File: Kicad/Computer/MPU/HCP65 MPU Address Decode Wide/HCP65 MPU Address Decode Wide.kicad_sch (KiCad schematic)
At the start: 0 parts

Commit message: Regenerating some gerbers again with paste layers.  Fixed Address Decode Wide.
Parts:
- added C23 (x10): 1μF, SamacSys_Parts:C_0805, symbol HCP65:C_0805
- added C27 (x2): 10μF, SamacSys_Parts:C_0805, symbol HCP65:C_0805
- added IC1: SN74LVC3G04DCUR, SOP50P310X90-8N, symbol Texas_Instruments:SN74LVC3G04DCUR_Multi
- added IC11, IC16, IC32, IC33, IC38, IC39: 74LVC138APW-Q100J, SOP65P640X110-16N, symbol Nexperia:74LVC138APW-Q100J
- added IC2: AP7365-33WG-7, SOT95P285X130-5N, symbol Diodes_Inc:AP7365-33WG-7
- added IC34: 74LVC1G27GW,125, SOP65P210X110-6N, symbol Nexperia:74LVC1G27GW,125
- added IC37: 74LVC2G32DP,125, SOP65P400X110-8N, symbol Nexperia:74LVC2G32DP,125_Multi
- added IC40: 74LVC08APW,112, SOP65P640X110-14N, symbol Nexperia:74LVC08APW,112_Multi
- added J1, J3: Pin_Header_01x32, SamacSys_Parts:PinHeader_1x32_P2.54mm_Vertical, symbol HCP65:Pin_Header_01x32
- added J2: Conn_02x32_Counter_Clockwise, SamacSys_Parts:DIP-64_Board_W15.24mm, symbol Connector_Generic:Conn_02x32_Counter_Clockwise
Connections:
- new net: IC37.5 (2A), IC40.8 (3Y)
- new net 3.3V: C23.1, C23.1, C23.1, C23.1, C23.1, C23.1, C23.1, C23.1, C23.1, C23.1, C27.1, IC1.8 (3V), IC1.8 (3V), IC1.8 (3V), IC11.16 (3V), IC16.16 (3V), IC2.5 (VOUT), IC32.16 (3V), IC33.16 (3V), IC34.5 (3V), IC37.8 (VCC), IC37.8 (VCC), IC38.16 (3V), IC39.16 (3V), IC40.14 (3V), IC40.14 (3V), IC40.14 (3V), IC40.14 (3V)
- new net 5V: C27.1, IC2.1 (VIN), IC2.3 (EN), J2.3 (Pin_3), J2.35 (Pin_35)
- new net A0: IC38.1 (A0), IC39.1 (A0), J2.24 (Pin_24)
- new net A1: IC38.2 (A1), IC39.2 (A1), J2.22 (Pin_22)
- new net A15: IC16.1 (A0), IC32.1 (A0), J2.19 (Pin_19)
- new net A16: IC16.2 (A1), IC32.2 (A1), J2.18 (Pin_18)
- new net A17: IC16.3 (A2), IC32.3 (A2), IC33.1 (A0), J2.17 (Pin_17)
- new net A18: IC16.5 (~{E2}), IC32.6 (E3), IC33.2 (A1), J2.16 (Pin_16)
- new net A19: IC11.1 (A0), J2.15 (Pin_15)
- new net A2: IC38.3 (A2), IC39.3 (A2), J2.21 (Pin_21)
- new net A20: IC11.2 (A1), J2.14 (Pin_14)
- new net A21: IC11.3 (A2), IC34.6 (C), J2.13 (Pin_13)
- new net A22: IC11.5 (~{E2}), IC34.3 (B), J2.12 (Pin_12)
- new net A23: IC11.4 (~{E1}), IC34.1 (A), J2.11 (Pin_11)
- new net A3: IC1.3 (2A), IC38.5 (~{E2}), J2.20 (Pin_20)
- new net GND: C23.2, C23.2, C23.2, C23.2, C23.2, C23.2, C23.2, C23.2, C23.2, C23.2, C27.2, C27.2, IC1.4 (GND), IC1.4 (GND), IC1.4 (GND), IC11.8 (GND), IC16.8 (GND), IC2.2 (GND), IC32.8 (GND), IC33.3 (A2), IC33.5 (~{E2}), IC33.8 (GND), IC34.2 (GND), IC37.4 (GND), IC37.4 (GND), IC38.8 (GND), IC39.8 (GND), IC40.7 (GND), IC40.7 (GND), IC40.7 (GND), IC40.7 (GND), J2.10 (Pin_10), J2.23 (Pin_23), J2.42 (Pin_42), J2.55 (Pin_55)
- new net Kernal Mode: IC40.1 (1A), IC40.10 (3B), J2.9 (Pin_9)
- new net Kernal Mode·Native Latch: IC11.6 (E3), IC40.3 (1Y)
- new net Native Latch: IC1.1 (1A), IC40.2 (1B), IC40.4 (2A), J2.2 (Pin_2)
- new net Reset: IC1.2 (3Y), IC32.5 (~{E2})
- new net ~{A21+A22+A23}: IC34.4 (Y), IC40.9 (3A)
- new net ~{A3}: IC1.5 (2Y), IC39.5 (~{E2})
- new net ~{Device Group 128K}: IC11.12 (~{Y3}), IC33.4 (~{E1}), IC40.13 (4B), J2.7 (Pin_7)
- new net ~{Device Group 32K}: IC11.13 (~{Y2}), IC16.4 (~{E1}), IC32.4 (~{E1}), IC40.12 (4A), J2.6 (Pin_6)
- new net ~{Device _{CS}10}: IC32.13 (~{Y2}), J2.52 (Pin_52)
- new net ~{Device _{CS}11}: IC32.12 (~{Y3}), J2.51 (Pin_51)
- new net ~{Device _{CS}12}: IC32.11 (~{Y4}), J2.50 (Pin_50)
- new net ~{Device _{CS}13}: IC32.10 (~{Y5}), J2.49 (Pin_49)
- new net ~{Device _{CS}14}: IC32.9 (~{Y6}), J2.48 (Pin_48)
- new net ~{Device _{CS}15}: IC32.7 (~{Y7}), J2.47 (Pin_47)
- new net ~{Device _{CS}16}: IC33.15 (~{Y0}), J2.46 (Pin_46)
- new net ~{Device _{CS}17}: IC33.14 (~{Y1}), J2.45 (Pin_45)
- new net ~{Device _{CS}18}: IC33.13 (~{Y2}), J2.44 (Pin_44)
- new net ~{Device _{CS}19}: IC33.12 (~{Y3}), J2.43 (Pin_43)
- new net ~{Device _{CS}1}: IC16.14 (~{Y1}), J2.63 (Pin_63)
- new net ~{Device _{CS}2}: IC16.13 (~{Y2}), J2.61 (Pin_61)
- new net ~{Device _{CS}3}: IC16.12 (~{Y3}), J2.60 (Pin_60)
- new net ~{Device _{CS}4}: IC16.11 (~{Y4}), J2.59 (Pin_59)
- new net ~{Device _{CS}5}: IC16.10 (~{Y5}), J2.58 (Pin_58)
- new net ~{Device _{CS}6}: IC16.9 (~{Y6}), J2.57 (Pin_57)
- new net ~{Device _{CS}7}: IC16.7 (~{Y7}), J2.56 (Pin_56)
- new net ~{Device _{CS}8}: IC32.15 (~{Y0}), J2.54 (Pin_54)
- new net ~{Device _{CS}9}: IC32.14 (~{Y1}), J2.53 (Pin_53)
- new net ~{Device}: IC40.11 (4Y), J2.1 (Pin_1)
- new net ~{Native Latch}: IC1.7 (1Y), IC37.1 (1A), IC37.6 (2B)
- new net ~{OTHER}: IC37.3 (2Y), J2.8 (Pin_8)
- new net ~{RAM_{CS}}: IC37.7 (1Y), J2.4 (Pin_4)
- new net ~{RAM}: IC11.15 (~{Y0}), IC37.2 (1B)
- new net ~{ROM_{CS}}: IC40.6 (2Y), J2.5 (Pin_5)
- new net ~{ROM}: IC11.14 (~{Y1}), IC40.5 (2B)
- new net ~{Reset}: IC1.6 (3A), IC16.6 (E3), IC33.6 (E3), IC38.6 (E3), IC39.6 (E3), J2.62 (Pin_62)
- new net ~{SPECIAL}: IC16.15 (~{Y0}), IC38.4 (~{E1}), IC39.4 (~{E1}), J2.64 (Pin_64)
- new net ~{Special _{CS}0}: IC38.15 (~{Y0}), J2.41 (Pin_41)
- new net ~{Special _{CS}10}: IC39.13 (~{Y2}), J2.27 (Pin_27)
- new net ~{Special _{CS}11}: IC39.12 (~{Y3}), J2.28 (Pin_28)
- new net ~{Special _{CS}12}: IC39.11 (~{Y4}), J2.29 (Pin_29)
- new net ~{Special _{CS}13}: IC39.10 (~{Y5}), J2.30 (Pin_30)
- new net ~{Special _{CS}14}: IC39.9 (~{Y6}), J2.31 (Pin_31)
- new net ~{Special _{CS}15}: IC39.7 (~{Y7}), J2.32 (Pin_32)
- new net ~{Special _{CS}1}: IC38.14 (~{Y1}), J2.40 (Pin_40)
- new net ~{Special _{CS}2}: IC38.13 (~{Y2}), J2.39 (Pin_39)
- new net ~{Special _{CS}3}: IC38.12 (~{Y3}), J2.38 (Pin_38)
- new net ~{Special _{CS}4}: IC38.11 (~{Y4}), J2.37 (Pin_37)
- new net ~{Special _{CS}5}: IC38.10 (~{Y5}), J2.36 (Pin_36)
- new net ~{Special _{CS}6}: IC38.9 (~{Y6}), J2.34 (Pin_34)
- new net ~{Special _{CS}7}: IC38.7 (~{Y7}), J2.33 (Pin_33)
- new net ~{Special _{CS}8}: IC39.15 (~{Y0}), J2.25 (Pin_25)
- new net ~{Special _{CS}9}: IC39.14 (~{Y1}), J2.26 (Pin_26)
- no-connect marks 0 -> 9
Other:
- removed sheet Address Decode Board
- note added: "A19..A23 Decode"
- note added: "Device Select"
- note added: "Kernal Mode Inverse"
- note added: "Other Select"
- note added: "Power and Spares"
- note added: "Special Address Select"
- title: (none) -> MPU Address Decode Wide

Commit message: Generated Gerbers for MPU components.
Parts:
- IC1: footprint SOP50P310X90-8N -> SamacSys_Parts:SOP50P310X90-8N; Garbage (none) -> TRIPLE INVERTER GATE
- IC11, IC16, IC32, IC33, IC38, IC39: footprint SOP65P640X110-16N -> SamacSys_Parts:SOP65P640X110-16N; Garbage (none) -> 74LVC138A-Q100 - 3-to-8 line decoder/demultiplexer; inverti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
- IC2: footprint SOT95P285X130-5N -> SamacSys_Parts:SOT95P285X130-5N
- IC34: footprint SOP65P210X110-6N -> SamacSys_Parts:SOP65P210X110-6N; Garbage (none) -> 74LVC1G27 - Single 3-input NOR gate@en-us
- IC37: footprint SOP65P400X110-8N -> SamacSys_Parts:SOP65P400X110-8N; Garbage (none) -> Nexperia 74LVC2G32DP,125, Dual 2-Input OR Logic Gate, 8-Pin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
- IC40: footprint SOP65P640X110-14N -> SamacSys_Parts:SOP65P640X110-14N; Garbage (none) -> NXP 74LVC08APW,112, Quad 2-Input AND Logic Gate, 1.2 3.6 V,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

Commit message: Removed MPU copper fills.
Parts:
- IC11, IC16, IC32, IC33, IC38, IC39: Garbage 74LVC138A-Q100 - 3-to-8 line decoder/demultiplexer; inverti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 -> (none)
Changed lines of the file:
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@@
 		)
 		(property "Footprint" "SamacSys_Parts:SOP65P640X110-16N"
-			(at 357.505 191.135 0)
+			(at 358.14 191.77 0)
 			(effects
 				(font
@@
 		)
 		(property "Datasheet" "https://assets.nexperia.com/documents/data-sheet/74LVC138A_Q100.pdf"
-			(at 357.505 193.675 0)
+			(at 358.14 194.31 0)
 			(effects
 				(font
@@
 		)
 		(property "Height" "1.1"
-			(at 357.505 198.755 0)
+			(at 358.14 199.39 0)
 			(effects
 				(font
@@
 		)
 		(property "Mouser Part Number" "771-74LVC138APWQ100J"
-			(at 357.505 201.295 0)
+			(at 358.14 201.93 0)
 			(effects
 				(font
@@
 		)
 		(property "Mouser Price/Stock" "https://www.mouser.co.uk/ProductDetail/Nexperia/74LVC138APW-Q100J?qs=fi7yB2oewZnXKE82xo%252BhJQ%3D%3D"
-			(at 357.505 203.835 0)
+			(at 358.14 204.47 0)
 			(effects
 				(font
@@
 		)
 		(property "Manufacturer_Name" "Nexperia"
-			(at 357.505 206.375 0)
+			(at 358.14 207.01 0)
 			(effects
 				(font
@@
 		)
 		(property "Manufacturer_Part_Number" "74LVC138APW-Q100J"
-			(at 357.505 208.915 0)
+			(at 358.14 209.55 0)
 			(effects
 				(font
@@
 		)
 		(property "Silkscreen" "74LVC138"
-			(at 341.63 187.96 0)
-			(effects
-				(font
-					(size 1.27 1.27)
-				)
-				(hide yes)
-			)
-		)
-		(property "Garbage" "74LVC138A-Q100 - 3-to-8 line decoder/demultiplexer; inverting@en-us"
-			(at 328.93 160.655 0)
-			(effects
-				(font
-					(size 1.27 1.27)
-				)
+			(at 358.14 196.85 0)
+			(effects
+				(font
+					(size 1.27 1.27)
+				)
+				(justify left)
 				(hide yes)
 			)
@@
 		)
 		(property "Footprint" "SamacSys_Parts:SOP65P640X110-16N"
-			(at 358.775 57.785 0)
+			(at 359.41 58.42 0)
 			(effects
 				(font
@@
 		)
 		(property "Datasheet" "https://assets.nexperia.com/documents/data-sheet/74LVC138A_Q100.pdf"
-			(at 358.775 60.325 0)
+			(at 359.41 60.96 0)
 			(effects
 				(font
@@
 		)
 		(property "Height" "1.1"
-			(at 358.775 65.405 0)
+			(at 359.41 66.04 0)
 			(effects
 				(font
@@
 		)
 		(property "Mouser Part Number" "771-74LVC138APWQ100J"
-			(at 358.775 67.945 0)
+			(at 359.41 68.58 0)
 			(effects
 				(font
@@
 		)
 		(property "Mouser Price/Stock" "https://www.mouser.co.uk/ProductDetail/Nexperia/74LVC138APW-Q100J?qs=fi7yB2oewZnXKE82xo%252BhJQ%3D%3D"
-			(at 358.775 70.485 0)
+			(at 359.41 71.12 0)
 			(effects
 				(font
@@
 		)
 		(property "Manufacturer_Name" "Nexperia"
-			(at 358.775 73.025 0)
+			(at 359.41 73.66 0)
 			(effects
 				(font
@@
 		)
 		(property "Manufacturer_Part_Number" "74LVC138APW-Q100J"
-			(at 358.775 75.565 0)
+			(at 359.41 76.2 0)
 			(effects
 				(font
@@
 		)
 		(property "Silkscreen" "74LVC138"
-			(at 342.9 54.61 0)
-			(effects
-				(font
-					(size 1.27 1.27)
-				)
-				(hide yes)
-			)
-		)
-		(property "Garbage" "74LVC138A-Q100 - 3-to-8 line decoder/demultiplexer; inverting@en-us"
-			(at 330.2 27.305 0)
-			(effects
-				(font
-					(size 1.27 1.27)
-				)
+			(at 359.41 63.5 0)
+			(effects
+				(font
+					(size 1.27 1.27)
+				)
+				(justify left)
 				(hide yes)
 			)
@@
 		)
 		(property "Footprint" "SamacSys_Parts:SOP65P640X110-16N"
-			(at 173.355 74.295 0)
+			(at 173.99 74.93 0)
 			(effects
 				(font
@@
 		)
 		(property "Datasheet" "https://assets.nexperia.com/documents/data-sheet/74LVC138A_Q100.pdf"
-			(at 173.355 76.835 0)
+			(at 173.99 77.47 0)
 			(effects
 				(font
@@
 		)
 		(property "Height" "1.1"
-			(at 173.355 81.915 0)
+			(at 173.99 82.55 0)
 			(effects
 				(font
@@
 		)
 		(property "Mouser Part Number" "771-74LVC138APWQ100J"
-			(at 173.355 84.455 0)
+			(at 173.99 85.09 0)
 			(effects
 				(font
@@
 		)
 		(property "Mouser Price/Stock" "https://www.mouser.co.uk/ProductDetail/Nexperia/74LVC138APW-Q100J?qs=fi7yB2oewZnXKE82xo%252BhJQ%3D%3D"
-			(at 173.355 86.995 0)
+			(at 173.99 87.63 0)
 			(effects
 				(font
@@
 		)
 		(property "Manufacturer_Name" "Nexperia"
-			(at 173.355 89.535 0)
+			(at 173.99 90.17 0)
 			(effects
 				(font
@@
 		)
 		(property "Manufacturer_Part_Number" "74LVC138APW-Q100J"
-			(at 173.355 92.075 0)
+			(at 173.99 92.71 0)
 			(effects
 				(font
@@
 		)
 		(property "Silkscreen" "74LVC138"
-			(at 157.48 71.12 0)
-			(effects
-				(font
-					(size 1.27 1.27)
-				)
-				(hide yes)
-			)
-		)
-		(property "Garbage" "74LVC138A-Q100 - 3-to-8 line decoder/demultiplexer; inverting@en-us"
-			(at 144.78 43.815 0)
-			(effects
-				(font
-					(size 1.27 1.27)
-				)
+			(at 173.99 80.01 0)
+			(effects
+				(font
+					(size 1.27 1.27)
+				)
+				(justify left)
 				(hide yes)
 			)
@@
 		)
 		(property "Footprint" "SamacSys_Parts:SOP65P640X110-16N"
-			(at 358.775 90.805 0)
+			(at 359.41 91.44 0)
 			(effects
 				(font
@@
 		)
 		(property "Datasheet" "https://assets.nexperia.com/documents/data-sheet/74LVC138A_Q100.pdf"
-			(at 358.775 93.345 0)
+			(at 359.41 93.98 0)
 			(effects
 				(font
@@
 		)
 		(property "Height" "1.1"
-			(at 358.775 98.425 0)
+			(at 359.41 99.06 0)
 			(effects
 				(font
@@
 		)
 		(property "Mouser Part Number" "771-74LVC138APWQ100J"
-			(at 358.775 100.965 0)
+			(at 359.41 101.6 0)
 			(effects
 				(font
@@
 		)
 		(property "Mouser Price/Stock" "https://www.mouser.co.uk/ProductDetail/Nexperia/74LVC138APW-Q100J?qs=fi7yB2oewZnXKE82xo%252BhJQ%3D%3D"
-			(at 358.775 103.505 0)
+			(at 359.41 104.14 0)
 			(effects
 				(font
@@
 		)
 		(property "Manufacturer_Name" "Nexperia"
-			(at 358.775 106.045 0)
+			(at 359.41 106.68 0)
 			(effects
 				(font
@@
 		)
 		(property "Manufacturer_Part_Number" "74LVC138APW-Q100J"
-			(at 358.775 108.585 0)
+			(at 359.41 109.22 0)
 			(effects
 				(font
@@
 		)
 		(property "Silkscreen" "74LVC138"
-			(at 342.9 87.63 0)
-			(effects
-				(font
-					(size 1.27 1.27)
-				)
-				(hide yes)
-			)
-		)
-		(property "Garbage" "74LVC138A-Q100 - 3-to-8 line decoder/demultiplexer; inverting@en-us"
-			(at 330.2 60.325 0)
-			(effects
-				(font
-					(size 1.27 1.27)
-				)
+			(at 359.41 96.52 0)
+			(effects
+				(font
+					(size 1.27 1.27)
+				)
+				(justify left)
 				(hide yes)
 			)
@@
 		)
 		(property "Footprint" "SamacSys_Parts:SOP65P640X110-16N"
-			(at 357.505 224.155 0)
+			(at 358.14 224.79 0)
 			(effects
 				(font
@@
 		)
 		(property "Datasheet" "https://assets.nexperia.com/documents/data-sheet/74LVC138A_Q100.pdf"
-			(at 357.505 226.695 0)
+			(at 358.14 227.33 0)
 			(effects
 				(font
@@
 		)
 		(property "Height" "1.1"
-			(at 357.505 231.775 0)
+			(at 358.14 232.41 0)
 			(effects
 				(font
@@
 		)
 		(property "Mouser Part Number" "771-74LVC138APWQ100J"
-			(at 357.505 234.315 0)
+			(at 358.14 234.95 0)
 			(effects
 				(font
@@
 		)
 		(property "Mouser Price/Stock" "https://www.mouser.co.uk/ProductDetail/Nexperia/74LVC138APW-Q100J?qs=fi7yB2oewZnXKE82xo%252BhJQ%3D%3D"
-			(at 357.505 236.855 0)
+			(at 358.14 237.49 0)
 			(effects
 				(font
@@
 		)
 		(property "Manufacturer_Name" "Nexperia"
-			(at 357.505 239.395 0)
+			(at 358.14 240.03 0)
 			(effects
 				(font
@@
 		)
 		(property "Manufacturer_Part_Number" "74LVC138APW-Q100J"
-			(at 357.505 241.935 0)
+			(at 358.14 242.57 0)
 			(effects
 				(font
@@
 		)
 		(property "Silkscreen" "74LVC138"
-			(at 341.63 220.98 0)
-			(effects
-				(font
-					(size 1.27 1.27)
-				)
-				(hide yes)
-			)
-		)
-		(property "Garbage" "74LVC138A-Q100 - 3-to-8 line decoder/demultiplexer; inverting@en-us"
-			(at 328.93 193.675 0)
-			(effects
-				(font
-					(size 1.27 1.27)
-				)
+			(at 358.14 229.87 0)
+			(effects
+				(font
+					(size 1.27 1.27)
+				)
+				(justify left)
 				(hide yes)
 			)
@@
 		)
 		(property "Footprint" "SamacSys_Parts:SOP65P640X110-16N"
-			(at 358.775 123.825 0)
+			(at 359.41 124.46 0)
 			(effects
 				(font
@@
 		)
 		(property "Datasheet" "https://assets.nexperia.com/documents/data-sheet/74LVC138A_Q100.pdf"
-			(at 358.775 126.365 0)
+			(at 359.41 127 0)
 			(effects
 				(font
@@
 		)
 		(property "Height" "1.1"
-			(at 358.775 131.445 0)
+			(at 359.41 132.08 0)
 			(effects
 				(font
@@
 		)
 		(property "Mouser Part Number" "771-74LVC138APWQ100J"
-			(at 358.775 133.985 0)
+			(at 359.41 134.62 0)
 			(effects
 				(font
@@
 		)
 		(property "Mouser Price/Stock" "https://www.mouser.co.uk/ProductDetail/Nexperia/74LVC138APW-Q100J?qs=fi7yB2oewZnXKE82xo%252BhJQ%3D%3D"
-			(at 358.775 136.525 0)
+			(at 359.41 137.16 0)
 			(effects
 				(font
@@
 		)
 		(property "Manufacturer_Name" "Nexperia"
-			(at 358.775 139.065 0)
+			(at 359.41 139.7 0)
 			(effects
 				(font
@@
 		)
 		(property "Manufacturer_Part_Number" "74LVC138APW-Q100J"
-			(at 358.775 141.605 0)
+			(at 359.41 142.24 0)
 			(effects
 				(font
@@
 		)
 		(property "Silkscreen" "74LVC138"
-			(at 342.9 120.65 0)
-			(effects
-				(font
-					(size 1.27 1.27)
-				)
-				(hide yes)
-			)
-		)
-		(property "Garbage" "74LVC138A-Q100 - 3-to-8 line decoder/demultiplexer; inverting@en-us"
-			(at 330.2 93.345 0)
-			(effects
-				(font
-					(size 1.27 1.27)
-				)
-				(hide yes)
-			)
+			(at 359.41 129.54 0)
+			(effects
+				(font
+					(size 1.27 1.27)
+				)
+				(justify left)
+				(hide yes)
+			)

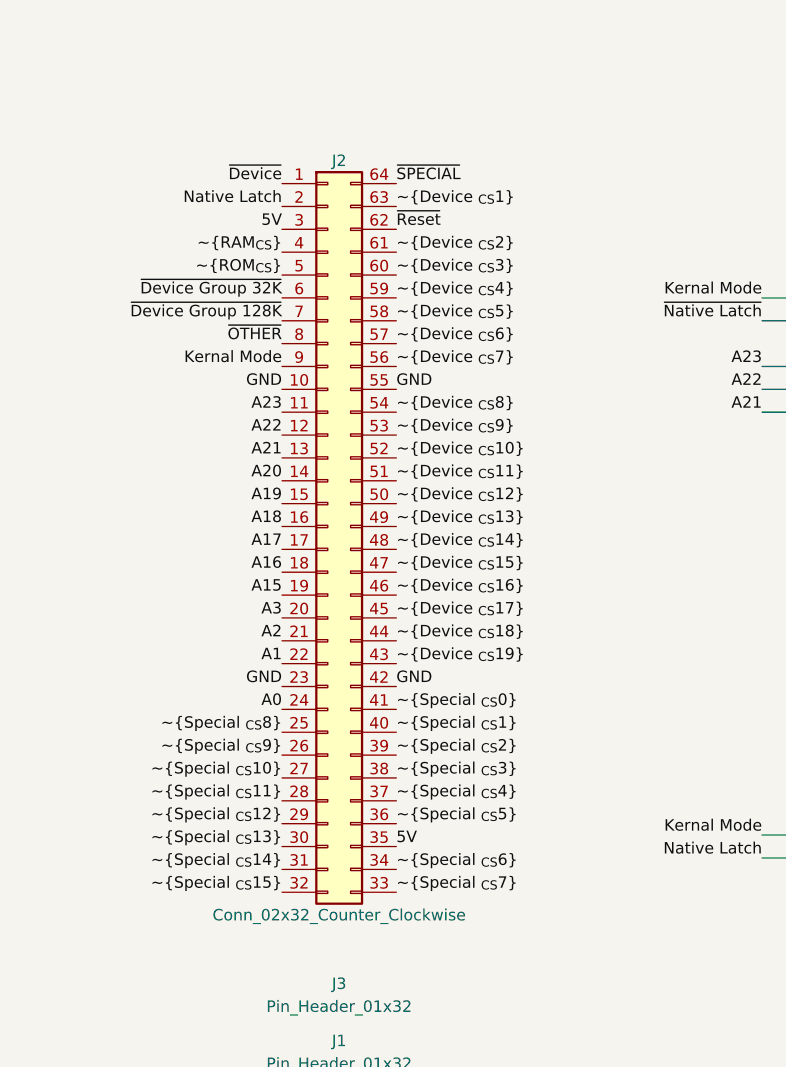
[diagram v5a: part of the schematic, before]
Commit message: Removed some component copper fills.
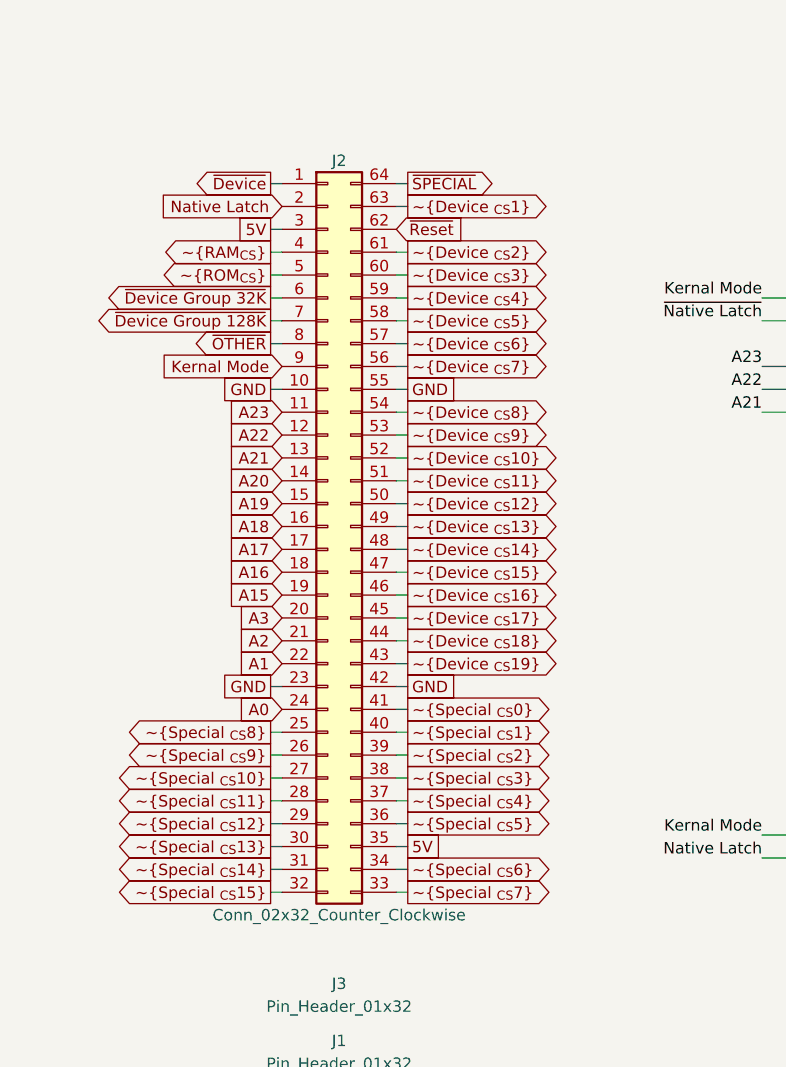
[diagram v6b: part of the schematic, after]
